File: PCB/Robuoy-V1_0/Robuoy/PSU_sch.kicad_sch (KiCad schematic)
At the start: 62 parts, among them J1 Accu/ESC_on-off, J5 TO FRONT SWITCH, Q1 MMBT2222A, Q2 MMBT2222A, Q201 NCE01P30K, Q3 MMBT2222A, U1 TPS5438PWP

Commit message: powersupply changes
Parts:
- removed C1: 4.7uF, A_Device:C_0603, symbol Device:C_Small
- removed C10: 6.8nF, symbol Device:C_Small
- removed C2: 330nF, symbol Device:C_Small
- removed C24: 100u/16V, Capacitor_SMD:C_1210_3225Metric, symbol Device:C_Small
- removed C6: 220u/50V, A_Device:CP_ALU_D10x10.5, symbol Device:C_Polarized_Small
- removed C9: 100n, A_Device:C_0603, symbol Device:C_Small
- removed D204: SS36-E3/57T, A_Device:D_SMC_7.1x6.2x2.65, symbol Device:D_Schottky_Small
- removed L3: 22uH/3A, A_Device:L_11.5x10.0mm, symbol Device:L_Small
- removed R1, R5: 3.3, symbol Device:R_Small
- removed R2, R6: 10, symbol Device:R_Small
- removed R3, R7: 20k, symbol Device:R_Small
- removed R4: 3.83k, symbol Device:R_Small
- removed R8: 6.34k, symbol Device:R_Small
- removed R9: 698, symbol Device:R_Small
- removed TP4, TP6, TP7, TP8: 5V, A_Pads_Pins:Testpoint_0.9x1.5, symbol Connector:TestPoint
- removed U1: TPS5438PWP, symbol missing_parts:TPS54383
- added C1, C10, C2, C9: 220u/50V, A_Device:CP_ALU_D10x10.5, symbol Device:C_Polarized_Small
- added C19: 100n, A_Device:C_0603, symbol Device:C_Small
- added C6: 100u/16V, Capacitor_SMD:C_1210_3225Metric, symbol Device:C_Small
- added D6: SS36-E3/57T, A_Device:D_SMC_7.1x6.2x2.65, symbol Device:D_Schottky_Small
- added L2: 68uH/3A, A_Device:L_11.5x10.0mm, symbol Device:L_Small
- added U1: LM2595S-5, Package_TO_SOT_SMD:TO-263-5_TabPin3, symbol Regulator_Switching:LM2595S-5
- added U5: LM2595S-3.3, Package_TO_SOT_SMD:TO-263-5_TabPin3, symbol Regulator_Switching:LM2595S-3.3
- C11: value 330nF -> 100n; footprint (none) -> A_Device:C_0603; LCSC (none) -> C14663
- C12: value 470pF -> 100u/16V; footprint (none) -> Capacitor_SMD:C_1210_3225Metric; LCSC (none) -> C90143
- C14, C15, C4, C5: value 10u -> 100u/16V
- C3: value 1nF -> 100n; footprint (none) -> A_Device:C_0603; LCSC (none) -> C14663
- C7: value 100n -> 100u/16V; footprint A_Device:C_0603 -> Capacitor_SMD:C_1210_3225Metric; LCSC C14663 -> C90143
- C8: value 10u -> 100n; footprint Capacitor_SMD:C_1210_3225Metric -> A_Device:C_0603; LCSC C90143 -> C14663
- L1: value 2.2uH/2A -> 68uH/3A
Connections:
- net +28V: no longer C7.1
- net +3.3V: no longer C13.1, C14.1, C15.1, L1.2, TP3.1
- net +5V: now also C12.1, C13.1, C14.1, C15.1, C7.1, L1.2, TP3.1, TP5.1, C19.1, C6.1, L2.2, U1.1 (OUT)
- net GND: now also C11.2, C12.2, C3.2, C1.2, C10.2, C19.2, C2.2, C6.2, C9.2, D6.2 (A), U1.3 (GND), U1.5 (ON/~{OFF}); no longer R19.1
- net at C3.1: now also C1.1, C2.1, U1.2 (VIN)
- net at C11.1: now also C10.1, C9.1
- new net: D1.1 (K), L1.1, U1.4 (FB)
- new net: D6.1 (K), L2.1
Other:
- moved on the sheet: D201, Q201, R19

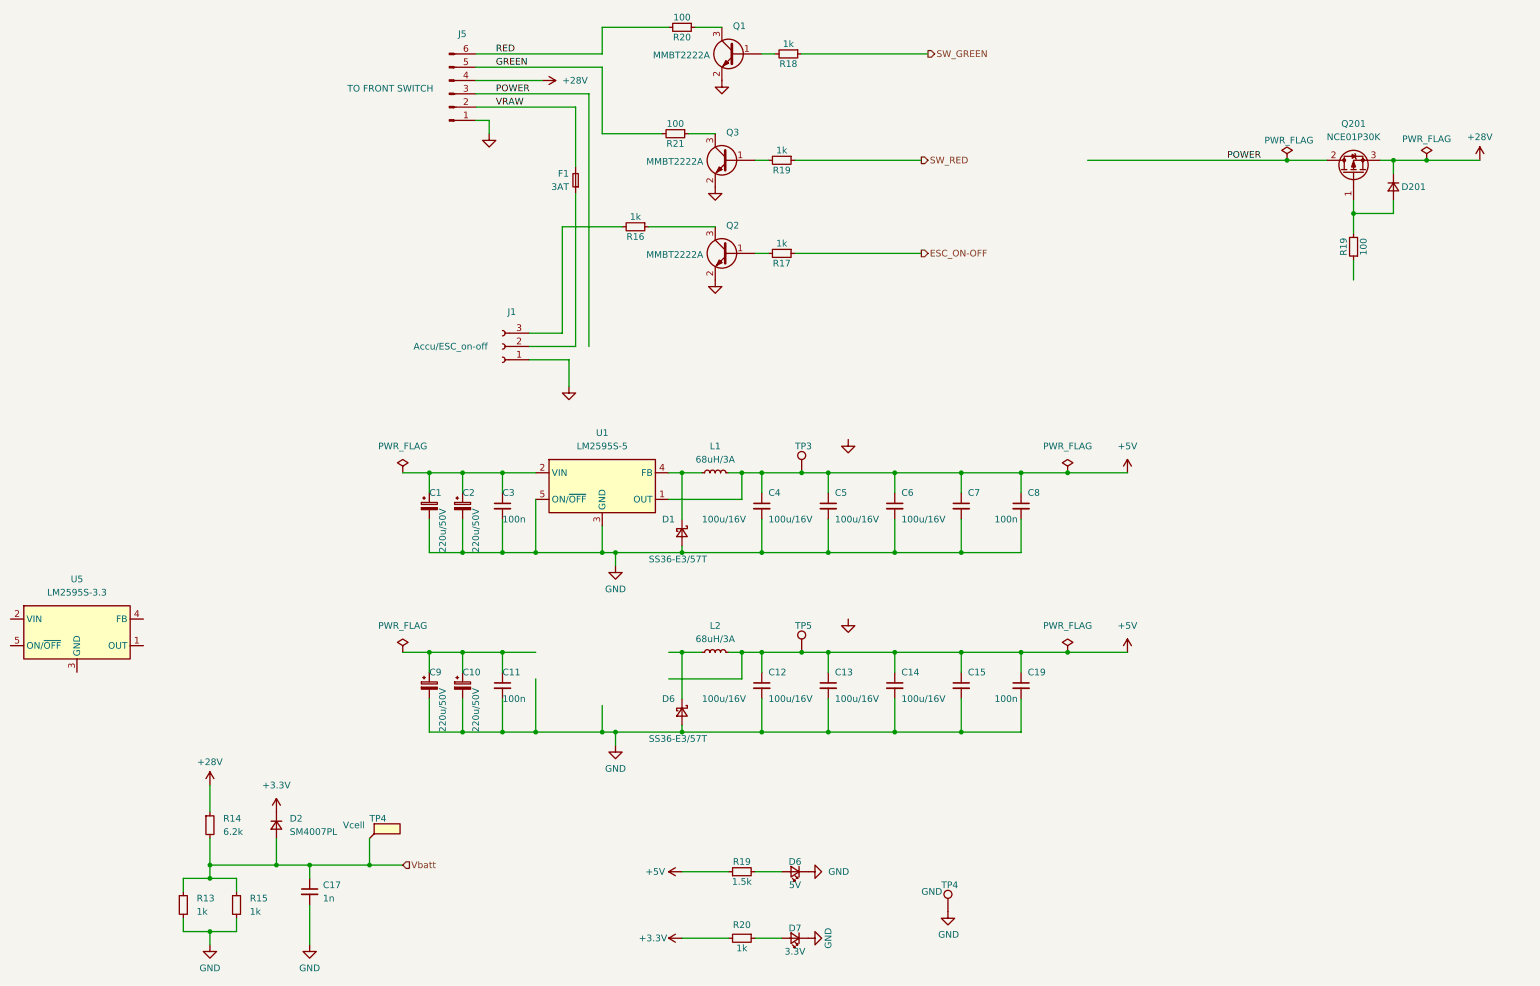
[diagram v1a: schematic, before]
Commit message: Schematics changed for new design
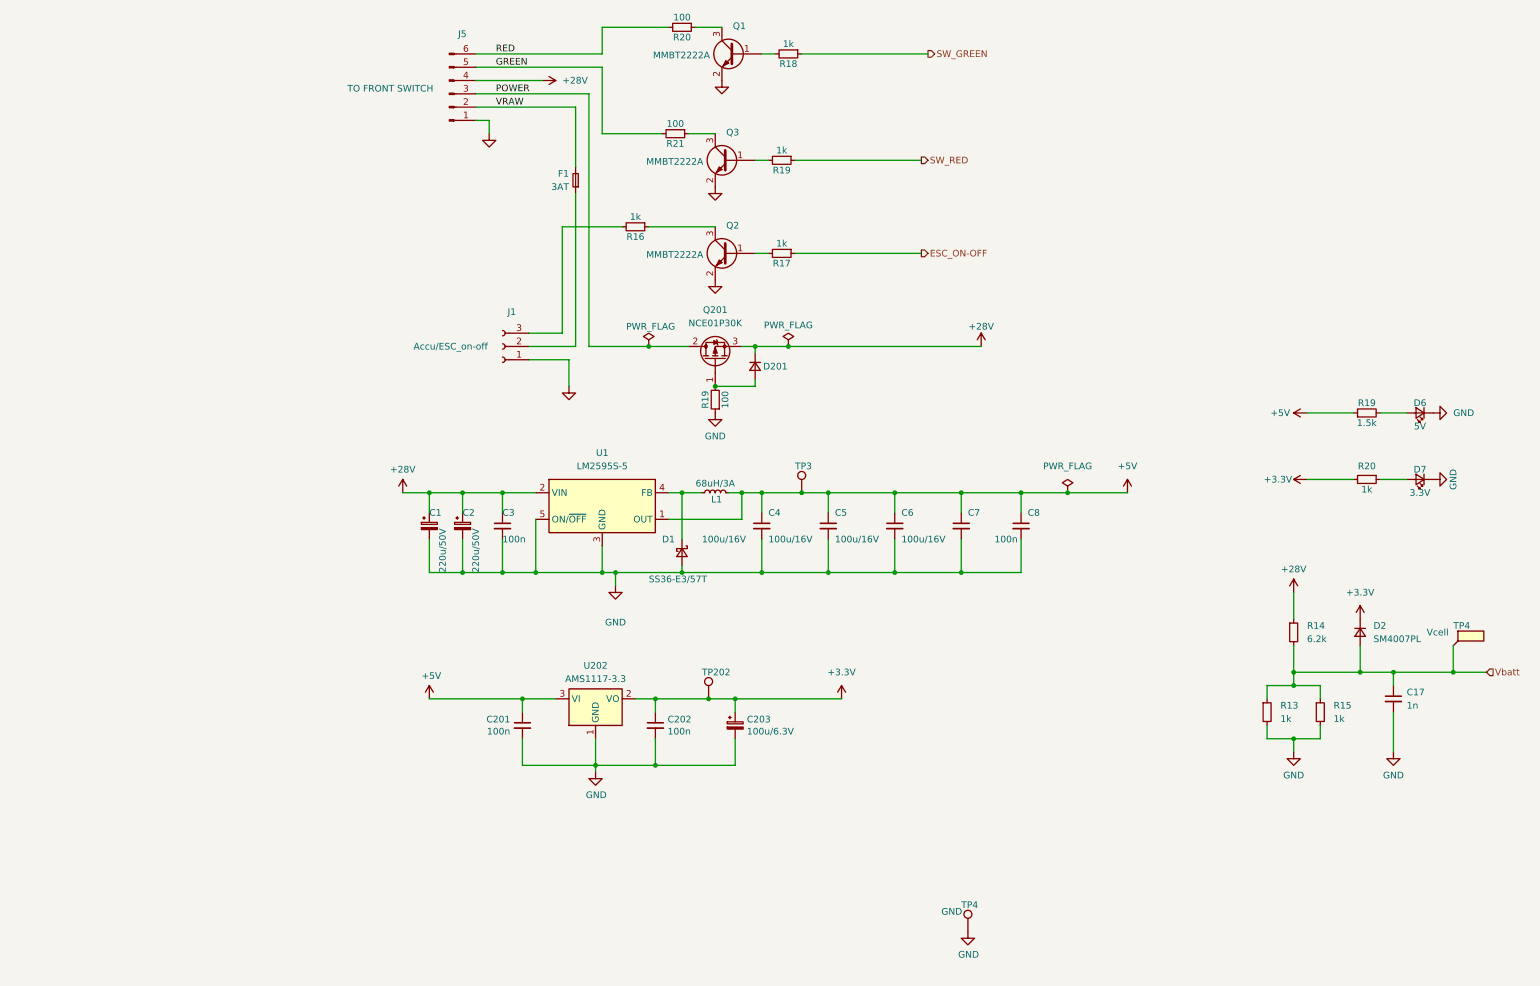
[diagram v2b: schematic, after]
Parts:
- removed C10, C9: 220u/50V, A_Device:CP_ALU_D10x10.5, symbol Device:C_Polarized_Small
- removed C11, C19: 100n, A_Device:C_0603, symbol Device:C_Small
- removed C12, C13, C14, C15: 100u/16V, Capacitor_SMD:C_1210_3225Metric, symbol Device:C_Small
- removed D6: SS36-E3/57T, A_Device:D_SMC_7.1x6.2x2.65, symbol Device:D_Schottky_Small
- removed L2: 68uH/3A, A_Device:L_11.5x10.0mm, symbol Device:L_Small
- removed TP5: 5V, A_Pads_Pins:Testpoint_0.9x1.5, symbol Connector:TestPoint
- removed U5: LM2595S-3.3, Package_TO_SOT_SMD:TO-263-5_TabPin3, symbol Regulator_Switching:LM2595S-3.3
- added C201, C202: 100n, A_Device:C_0603, symbol Device:C_Small
- added C203: 100u/6.3V, A_Device:CP_TANT_3.5x2.8x1.9, symbol Device:CP_Small
- added TP202: 3V3, A_Pads_Pins:Testpoint_0.9x1.5, symbol Connector:TestPoint
- added U202: AMS1117-3.3, Package_TO_SOT_SMD:SOT-223-3_TabPin2, symbol Regulator_Linear:AMS1117-3.3
- U1: LCSC (none) -> C5145315
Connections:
- net +28V: now also C1.1, C2.1, C3.1, U1.2 (VIN)
- net +3.3V: now also C202.1, C203.1, TP202.1, U202.2 (VO)
- net +5V: now also C201.1, U202.3 (VI)
- net GND: now also R19.1, C201.2, C202.2, C203.2, U202.1 (GND)
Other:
- moved on the sheet: C1, C17, C2, C3, C4, C5, C6, C7, C8, D1, D2, D201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

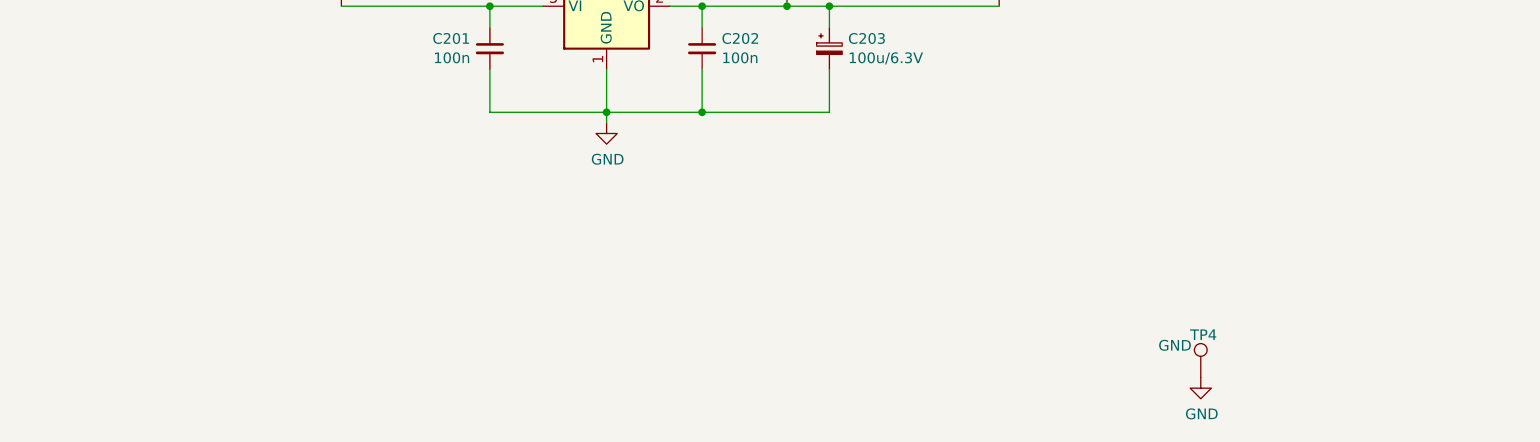
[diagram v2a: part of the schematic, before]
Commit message: Calibration restored after boot. This was the main issue! All good now
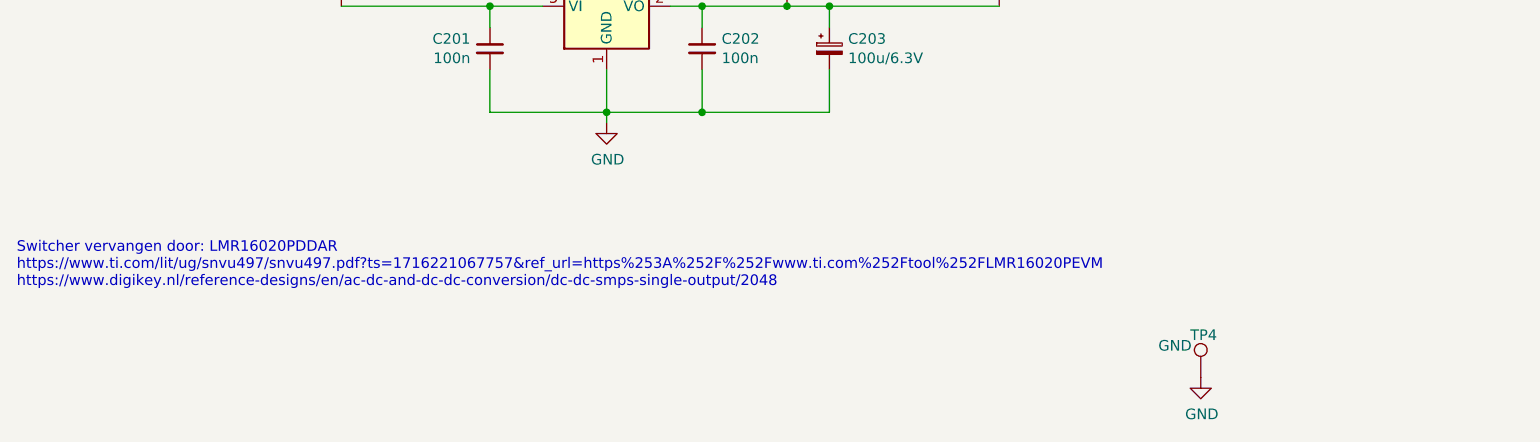
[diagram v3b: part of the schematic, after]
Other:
- note added: "Switcher vervangen door: LMR16020PDDAR https://www.ti.com/lit/ug/snvu497/snvu497.pdf?ts=1716221067757&ref_url=https%253A%252F%252Fwww.ti.com%252Ftool%252FLMR16020PEVM https://www.digikey.nl/reference-designs/en/ac-dc-and-dc-dc-conversion/dc-dc-smps-single-output/2048"
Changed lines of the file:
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@@
+		)
+	)
+	(text "Switcher vervangen door: LMR16020PDDAR\nhttps://www.ti.com/lit/ug/snvu497/snvu497.pdf?ts=1716221067757&ref_url=https%253A%252F%252Fwww.ti.com%252Ftool%252FLMR16020PEVM\nhttps://www.digikey.nl/reference-designs/en/ac-dc-and-dc-dc-conversion/dc-dc-smps-single-output/2048"
+		(exclude_from_sim no)
+		(at 28.448 175.768 0)
+		(effects
+			(font
+				(size 1.27 1.27)
+			)
+			(justify left)
+			(href "https://www.digikey.nl/reference-designs/en/ac-dc-and-dc-dc-conversion/dc-dc-smps-single-output/2048")
 		)
 	)

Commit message: auto calibrate
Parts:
- removed C1, C2: 220u/50V, A_Device:CP_ALU_D10x10.5, symbol Device:C_Polarized_Small
- removed C7: 100u/16V, Capacitor_SMD:C_1210_3225Metric, symbol Device:C_Small
- removed D1: SS36-E3/57T, A_Device:D_SMC_7.1x6.2x2.65, symbol Device:D_Schottky_Small
- removed U1: LM2595S-5, Package_TO_SOT_SMD:TO-263-5_TabPin3, symbol Regulator_Switching:LM2595S-5
- added C1, C2, C9: 2.2uF/50V, A_Device:C_0603, symbol Device:C_Small
- added C10: 100n, A_Device:C_0603, symbol Device:C_Small
- added D3: B360B-13-F, Diode_SMD:D_SMB, symbol Device:D_Schottky_Small
- added R1: 7.5k, A_Device:R_0603, symbol Device:R_Small
- added R2: 1.3k, A_Device:R_0603, symbol Device:R_Small
- C3: value 100n -> 470nF/50V; LCSC C14663 -> C513651
- C4, C5: value 100u/16V -> 47u/10V; footprint Capacitor_SMD:C_1210_3225Metric -> Capacitor_SMD:C_1206_3216Metric; LCSC C90143 -> C96123
- C6: value 100u/16V -> 1uF/50V; footprint Capacitor_SMD:C_1210_3225Metric -> Capacitor_SMD:C_0603_1608Metric; LCSC C90143 -> C1584
- L1: value 68uH/3A -> 10uH/3A; footprint A_Device:L_11.5x10.0mm -> Inductor_SMD:L_Neosid_Air-Coil_SML_6-10turn_HAM0631A-HAM1031A; LCSC C497902 -> C408412
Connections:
- net +28V: now also C1.1, C2.1, C9.1
- net +5V: now also R1.2
- net GND: now also C1.2, C2.2, C9.2, D3.2 (A)
- net at L1.1: now also C10.2, D3.1 (K)
- new net: R1.1, R2.2
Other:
- moved on the sheet: C3, C4, C8, L1, TP3

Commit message: Minor changes in pcb
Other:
- note added: "3.3V power supply TPS54331"
- note added: "Step up concerete 700mA TLV61046ADBVR https://jlcpcb.com/partdetail/TexasInstruments-TLV61046ADBVR/C464815"
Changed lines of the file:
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@@
+		)
+	)
+	(text "3.3V power supply\nTPS54331"
+		(exclude_from_sim no)
+		(at 29.21 183.642 0)
+		(effects
+			(font
+				(size 1.27 1.27)
+			)
 		)
 	)
@@
 		)
 	)
+	(text "Step up concerete 700mA\nTLV61046ADBVR\n\nhttps://jlcpcb.com/partdetail/TexasInstruments-TLV61046ADBVR/C464815"
+		(exclude_from_sim no)
+		(at 62.484 186.182 0)
+		(effects
+			(font
+				(size 1.27 1.27)
+			)
+		)
+	)
